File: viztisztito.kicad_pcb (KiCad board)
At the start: 2 copper layers, 110 x 102 mm, 77 parts, among them P1 BOARD_CONN, Q1 BC850, U1 VTX-214-010-205, U2 LTV-847, U3 ACS722, U4 MCP3004, U5 TC77

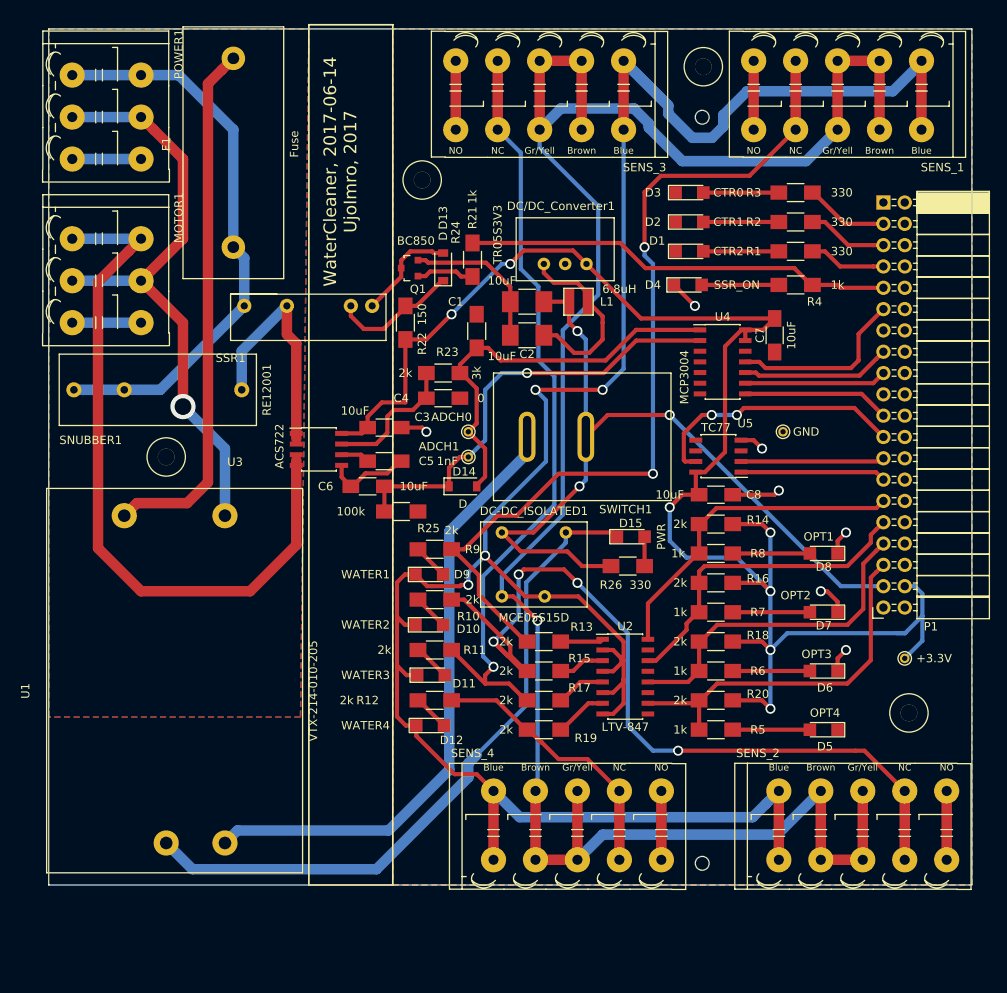
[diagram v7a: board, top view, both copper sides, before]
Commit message: final changes:
- fuse fix
- annotation on the connectors water
- annotation on the connectors power
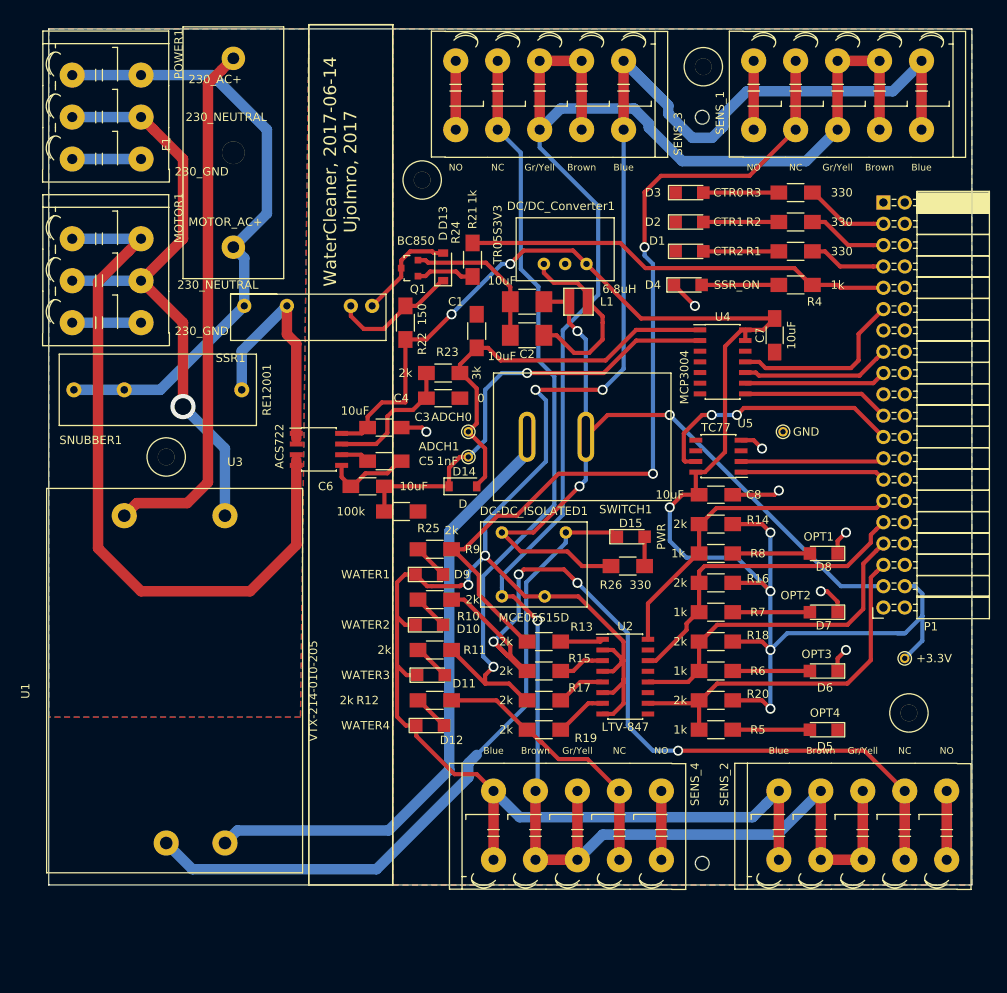
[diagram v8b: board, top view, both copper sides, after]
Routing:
- net 230V_AC+: track 67.9 -> 73.5 mm
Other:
- board text added: "230_AC+"
- board text added: "230_GND"
- board text added: "230_NEUTRAL"
- board text added: "MOTOR_AC+"
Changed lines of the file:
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@@
     (links 179)
     (no_connects 0)
-    (area 20.225 20.166666 142.880315 128.67626)
+    (area 19.455 20.166666 142.880315 128.67626)
     (thickness 1.6)
-    (drawings 29)
-    (tracks 558)
+    (drawings 35)
+    (tracks 559)
     (zones 0)
     (modules 77)
@@
     )
   )
-  (module water:FUSE-0031.8201 (layer F.Cu)
-    (at 52 22.75 270)
-    (fp_text reference F1 (at 13.97 13.97 270) (layer F.SilkS)
-      (effects (font (size 1 1) (thickness 0.15)))
-    )
-    (fp_text value Fuse (at 13.97 -1.27 270) (layer F.SilkS)
-      (effects (font (size 1 1) (thickness 0.15)))
-    )
-    (fp_line (start 0 0) (end 30 0) (layer F.SilkS) (width 0.15))
-    (fp_line (start 30 0) (end 30 12) (layer F.SilkS) (width 0.15))
-    (fp_line (start 30 12) (end 0 12) (layer F.SilkS) (width 0.15))
-    (fp_line (start 0 12) (end 0 0) (layer F.SilkS) (width 0.15))
-    (pad 1 thru_hole circle (at 3.75 6 270) (size 2.8 2.8) (drill 1.4) (layers *.Cu *.Mask)
-      (net 25 "Net-(F1-Pad1)"))
-    (pad 2 thru_hole circle (at 26.25 6 270) (size 2.8 2.8) (drill 1.4) (layers *.Cu *.Mask)
-      (net 26 230V_AC+))
-  )
   (module water:SRN3012TA-6R8M (layer F.Cu)
     (at 88.875 57.1 180)
@@
       (effects (font (size 1 1) (thickness 0.1)))
     )
-    (fp_text value PF240D25 (at 0 -0.5) (layer F.Fab)
+    (fp_text value PF240D25 (at 0 -0.5) (layer F.Fab) hide
       (effects (font (size 1 1) (thickness 0.1)))
     )
@@
   (module water:5x2_TerminalBlock_WAGO-2604-1105 (layer F.Cu)
     (at 130.49936 29.99874 180)
-    (fp_text reference SENS_1 (at 0 -9.5 180) (layer F.SilkS)
+    (fp_text reference SENS_1 (at 26.49936 -3.00126 270) (layer F.SilkS)
       (effects (font (size 1 1) (thickness 0.15)))
     )
@@
   (module water:5x2_TerminalBlock_WAGO-2604-1105 (layer F.Cu)
     (at 108.50064 118.80126)
-    (fp_text reference SENS_2 (at 0 -9.5) (layer F.SilkS)
+    (fp_text reference SENS_2 (at -4.00064 -5.80126 90) (layer F.SilkS)
       (effects (font (size 1 1) (thickness 0.15)))
     )
@@
   (module water:5x2_TerminalBlock_WAGO-2604-1105 (layer F.Cu)
     (at 94.99936 29.99874 180)
-    (fp_text reference SENS_3 (at 0 -9.5 180) (layer F.SilkS)
+    (fp_text reference SENS_3 (at -4.00064 -5.50126 270) (layer F.SilkS)
       (effects (font (size 1 1) (thickness 0.15)))
     )
@@
   (module water:5x2_TerminalBlock_WAGO-2604-1105 (layer F.Cu)
     (at 74.50064 118.80126)
-    (fp_text reference SENS_4 (at 0 -9.5) (layer F.SilkS)
+    (fp_text reference SENS_4 (at 26.49936 -5.80126 90) (layer F.SilkS)
       (effects (font (size 1 1) (thickness 0.15)))
     )
@@
       (net 59 "Net-(SWITCH1-Pad1)"))
   )
+  (module water:FUSE-0031.8201 (layer F.Cu)
+    (at 52 22.75 270)
+    (fp_text reference F1 (at 13.97 13.97 270) (layer F.SilkS)
+      (effects (font (size 1 1) (thickness 0.15)))
+    )
+    (fp_text value Fuse (at 13.97 -1.27 270) (layer F.Fab)
+      (effects (font (size 1 1) (thickness 0.15)))
+    )
+    (fp_line (start 0 0) (end 30 0) (layer F.SilkS) (width 0.15))
+    (fp_line (start 30 0) (end 30 12) (layer F.SilkS) (width 0.15))
+    (fp_line (start 30 12) (end 0 12) (layer F.SilkS) (width 0.15))
+    (fp_line (start 0 12) (end 0 0) (layer F.SilkS) (width 0.15))
+    (pad 1 thru_hole circle (at 3.75 6 270) (size 2.8 2.8) (drill 1.4) (layers *.Cu *.Mask)
+      (net 25 "Net-(F1-Pad1)"))
+    (pad 2 thru_hole circle (at 26.25 6 270) (size 2.8 2.8) (drill 1.4) (layers *.Cu *.Mask)
+      (net 26 230V_AC+))
+    (pad "" thru_hole circle (at 15 6 270) (size 2.7 2.7) (drill 2.7) (layers *.Cu *.Mask))
+  )
+  (gr_text 230_GND (at 39 59) (layer F.SilkS)
+    (effects (font (size 1 1) (thickness 0.25)) (justify left))
+  )
+  (gr_text 230_NEUTRAL (at 49 53.5) (layer F.SilkS)
+    (effects (font (size 1 1) (thickness 0.25)) (justify right))
+  )
+  (gr_text MOTOR_AC+ (at 49.5 46) (layer F.SilkS)
+    (effects (font (size 1 1) (thickness 0.25)) (justify right))
+  )
+  (gr_text 230_GND (at 39 40) (layer F.SilkS)
+    (effects (font (size 1 1) (thickness 0.25)) (justify left))
+  )
+  (gr_text 230_NEUTRAL (at 50 33.5) (layer F.SilkS)
+    (effects (font (size 1 1) (thickness 0.25)) (justify right))
+  )
+  (gr_text 230_AC+ (at 47 29) (layer F.SilkS)
+    (effects (font (size 1 1) (thickness 0.25)) (justify right))
+  )
   (gr_text "WaterCleaner, 2017-06-14\nUjoImro, 2017" (at 58.75 40 90) (layer F.SilkS)
     (effects (font (size 1.5 1.5) (thickness 0.3)))
   )
-  (gr_text NO (at 131 111) (layer F.SilkS)
+  (gr_text NO (at 131 109) (layer F.SilkS)
     (effects (font (size 0.8 0.8) (thickness 0.1)))
   )
-  (gr_text NC (at 126 111) (layer F.SilkS)
+  (gr_text NC (at 126 109) (layer F.SilkS)
     (effects (font (size 0.8 0.8) (thickness 0.1)))
   )
-  (gr_text Gr/Yell (at 121 111) (layer F.SilkS)
+  (gr_text Gr/Yell (at 121 109) (layer F.SilkS)
     (effects (font (size 0.8 0.8) (thickness 0.1)))
   )
-  (gr_text Brown (at 116 111) (layer F.SilkS)
+  (gr_text Brown (at 116 109) (layer F.SilkS)
     (effects (font (size 0.8 0.8) (thickness 0.1)))
   )
-  (gr_text Blue (at 111 111) (layer F.SilkS)
+  (gr_text Blue (at 111 109) (layer F.SilkS)
     (effects (font (size 0.8 0.8) (thickness 0.1)))
   )
-  (gr_text NO (at 97 111) (layer F.SilkS)
+  (gr_text NO (at 97 109) (layer F.SilkS)
     (effects (font (size 0.8 0.8) (thickness 0.1)))
   )
-  (gr_text NC (at 92 111) (layer F.SilkS)
+  (gr_text NC (at 92 109) (layer F.SilkS)
     (effects (font (size 0.8 0.8) (thickness 0.1)))
   )
-  (gr_text Gr/Yell (at 87 111) (layer F.SilkS)
+  (gr_text Gr/Yell (at 87 109) (layer F.SilkS)
     (effects (font (size 0.8 0.8) (thickness 0.1)))
   )
-  (gr_text Brown (at 82 111) (layer F.SilkS)
+  (gr_text Brown (at 82 109) (layer F.SilkS)
     (effects (font (size 0.8 0.8) (thickness 0.1)))
   )
-  (gr_text Blue (at 77 111) (layer F.SilkS)
+  (gr_text Blue (at 77 109) (layer F.SilkS)
     (effects (font (size 0.8 0.8) (thickness 0.1)))
   )
-  (gr_text NO (at 72.5 37.5) (layer F.SilkS)
+  (gr_text NO (at 72.5 39.5) (layer F.SilkS)
     (effects (font (size 0.8 0.8) (thickness 0.1)))
   )
-  (gr_text NC (at 77.5 37.5) (layer F.SilkS)
+  (gr_text NC (at 77.5 39.5) (layer F.SilkS)
     (effects (font (size 0.8 0.8) (thickness 0.1)))
   )
-  (gr_text Gr/Yell (at 82.5 37.5) (layer F.SilkS)
+  (gr_text Gr/Yell (at 82.5 39.5) (layer F.SilkS)
     (effects (font (size 0.8 0.8) (thickness 0.1)))
   )
-  (gr_text Brown (at 87.5 37.5) (layer F.SilkS)
+  (gr_text Brown (at 87.5 39.5) (layer F.SilkS)
     (effects (font (size 0.8 0.8) (thickness 0.1)))
   )
-  (gr_text Blue (at 92.5 37.5) (layer F.SilkS)
+  (gr_text Blue (at 92.5 39.5) (layer F.SilkS)
     (effects (font (size 0.8 0.8) (thickness 0.1)))
   )
-  (gr_text NO (at 108 37.5) (layer F.SilkS)
+  (gr_text NO (at 108 39.5) (layer F.SilkS)
     (effects (font (size 0.8 0.8) (thickness 0.1)))
   )
-  (gr_text NC (at 113 37.5) (layer F.SilkS)
+  (gr_text NC (at 113 39.5) (layer F.SilkS)
     (effects (font (size 0.8 0.8) (thickness 0.1)))
   )
-  (gr_text Gr/Yell (at 118 37.5) (layer F.SilkS)
+  (gr_text Gr/Yell (at 118 39.5) (layer F.SilkS)
     (effects (font (size 0.8 0.8) (thickness 0.1)))
   )
-  (gr_text Blue (at 128 37.5) (layer F.SilkS)
+  (gr_text Blue (at 128 39.5) (layer F.SilkS)
     (effects (font (size 0.8 0.8) (thickness 0.1)))
   )
-  (gr_text Brown (at 123 37.5) (layer F.SilkS)
+  (gr_text Brown (at 123 39.5) (layer F.SilkS)
     (effects (font (size 0.8 0.8) (thickness 0.1)))
   )
@@
   (segment (start 42.974999 29.525001) (end 44.600001 27.899999) (width 1.25) (layer F.Cu) (net 25))
   (segment (start 44.600001 27.899999) (end 46 26.5) (width 1.25) (layer F.Cu) (net 25))
+  (segment (start 35.00126 28.49936) (end 43.49936 28.49936) (width 1.25) (layer B.Cu) (net 26))
+  (segment (start 43.49936 28.49936) (end 50 35) (width 1.25) (layer B.Cu) (net 26))
+  (segment (start 50 35) (end 50 45) (width 1.25) (layer B.Cu) (net 26))
+  (segment (start 50 45) (end 46 49) (width 1.25) (layer B.Cu) (net 26))
   (segment (start 33 66) (end 37.3 66) (width 1.25) (layer B.Cu) (net 26))
   (segment (start 37.3 66) (end 47.3 56) (width 1.25) (layer B.Cu) (net 26))
   (segment (start 27 66) (end 33 66) (width 1.25) (layer B.Cu) (net 26))
-  (segment (start 46 35) (end 46 49) (width 1.25) (layer B.Cu) (net 26))
-  (segment (start 39.49936 28.49936) (end 46 35) (width 1.25) (layer B.Cu) (net 26))
-  (segment (start 35.00126 28.49936) (end 39.49936 28.49936) (width 1.25) (layer B.Cu) (net 26))
   (segment (start 47.3 56) (end 47.3 50.3) (width 1.25) (layer B.Cu) (net 26))
   (segment (start 47.3 50.3) (end 46 49) (width 1.25) (layer B.Cu) (net 26))
